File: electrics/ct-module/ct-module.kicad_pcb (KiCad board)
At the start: 2 copper layers, 86 x 31 mm, 43 parts, among them J1 North, J3 West, J4 East, J5 SJ1-3533NG, J6 SJ1-3533NG, J7 SJ1-3533NG, U1 BA033CC0FP-E2, U2 ADS1115IDGS, U3 MAX3486

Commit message: Review Fixes
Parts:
- removed D4, D8, D9: 3V3, Diode_SMD:D_SOD-523
- D1: footprint Diode_SMD:D_SOD-523 -> Diode_SMD:D_SOD-123
- D10, D5, D6, D7: value TVS -> 3V3
- D3: value D_TVS -> 3V3
- U2: footprint Package_SO:TSSOP-10_3x3mm_P0.5mm -> Package_SO:VSSOP-10_3x3mm_P0.5mm
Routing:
- net CT_2_K: track 60.0 -> 57.7 mm
- net CT_1_K: track 56.2 -> 54.3 mm
- net CT_0_K: track 60.6 -> 58.8 mm
- net GND: track 11.9 -> 10.9 mm
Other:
- board text added: "SR-CT-020"
- board text removed: "SR-ME-020"

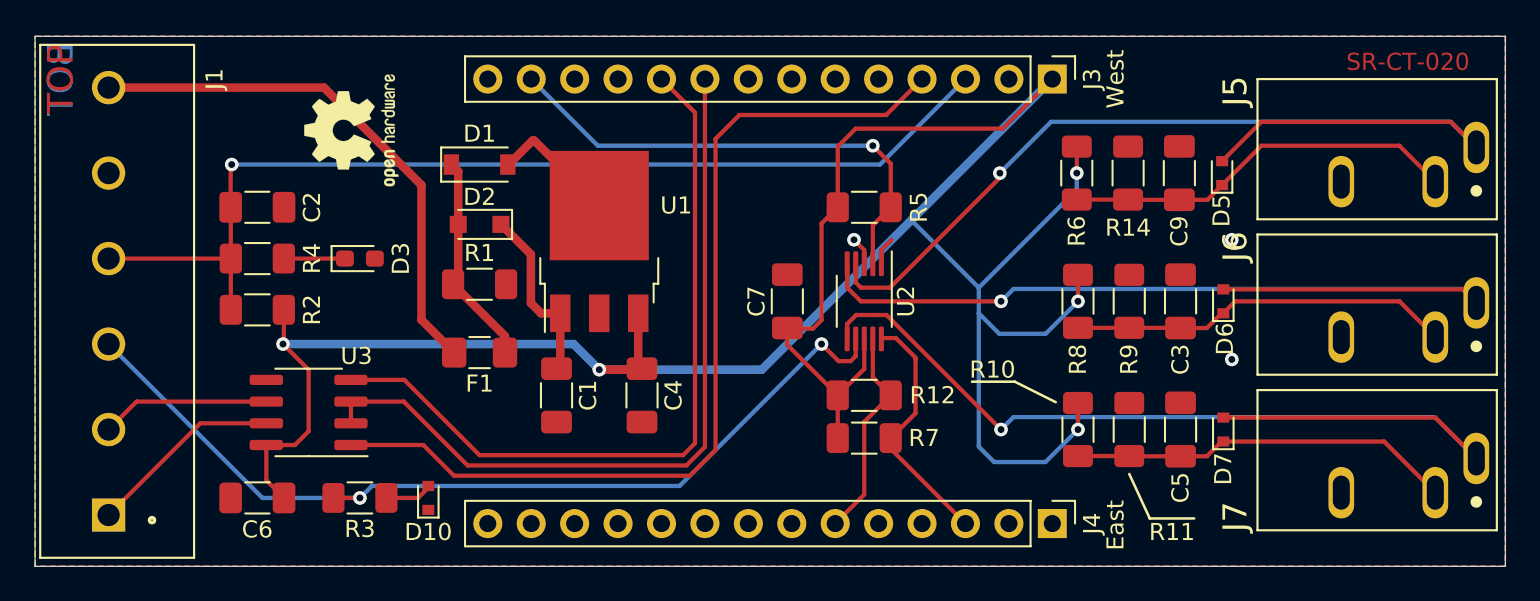
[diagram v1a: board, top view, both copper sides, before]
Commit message: INOA-372 Finalize CT module
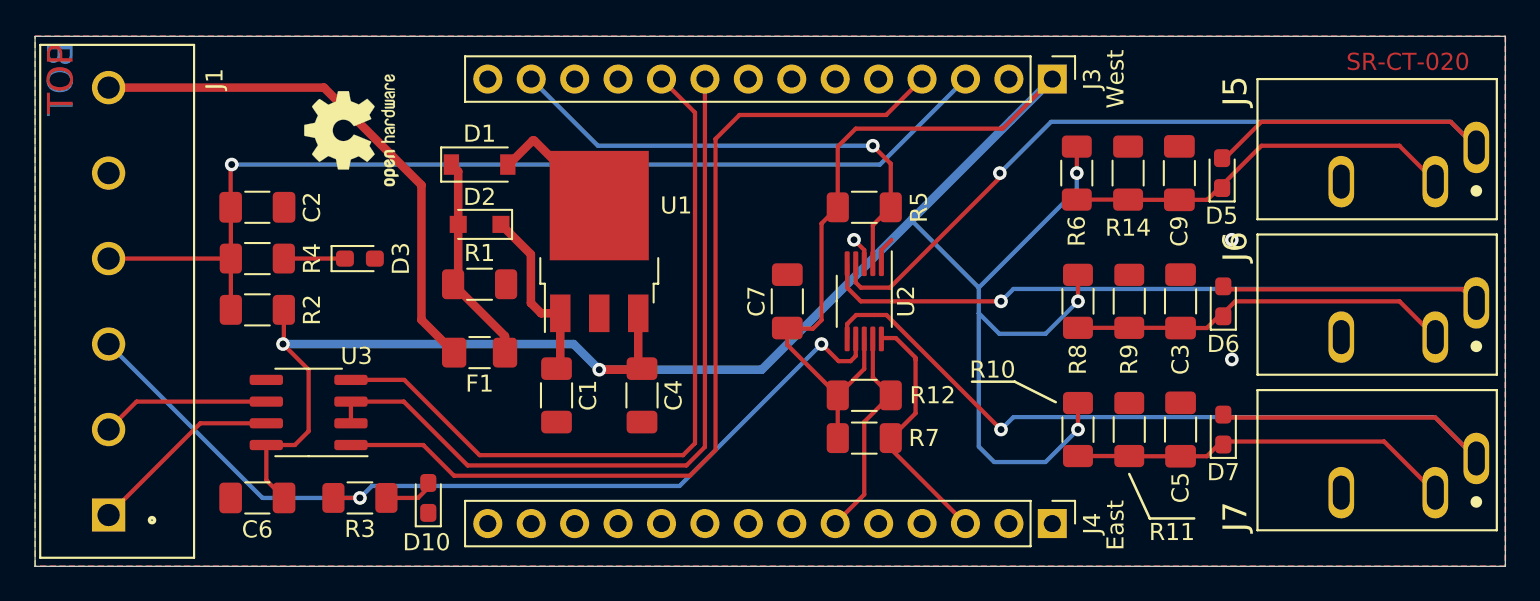
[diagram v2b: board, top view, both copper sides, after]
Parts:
- D10, D5, D6, D7: footprint Diode_SMD:D_SOD-523 -> Diode_SMD:D_0603_1608Metric_Pad1.05x0.95mm_HandSolder
